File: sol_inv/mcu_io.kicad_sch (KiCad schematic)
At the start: 33 parts, among them J10 Conn_01x05, J3 Conn_01x06, J4 Conn_01x05, J5 Conn_ARM_JTAG_SWD_10, J6 Conn_01x02, J7 Conn_01x08, J8 Conn_01x08, J9 Conn_01x05, SW2 SW_Push_Dual, SW3 SW_Push_Dual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

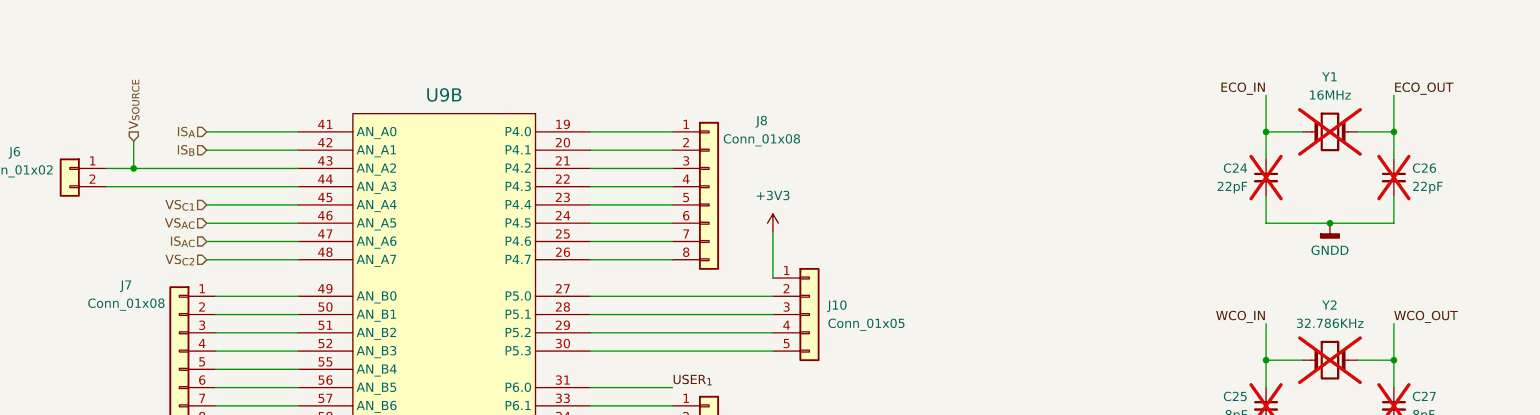
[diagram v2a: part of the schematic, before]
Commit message: v0.3 pcb layout pre-drc fixes
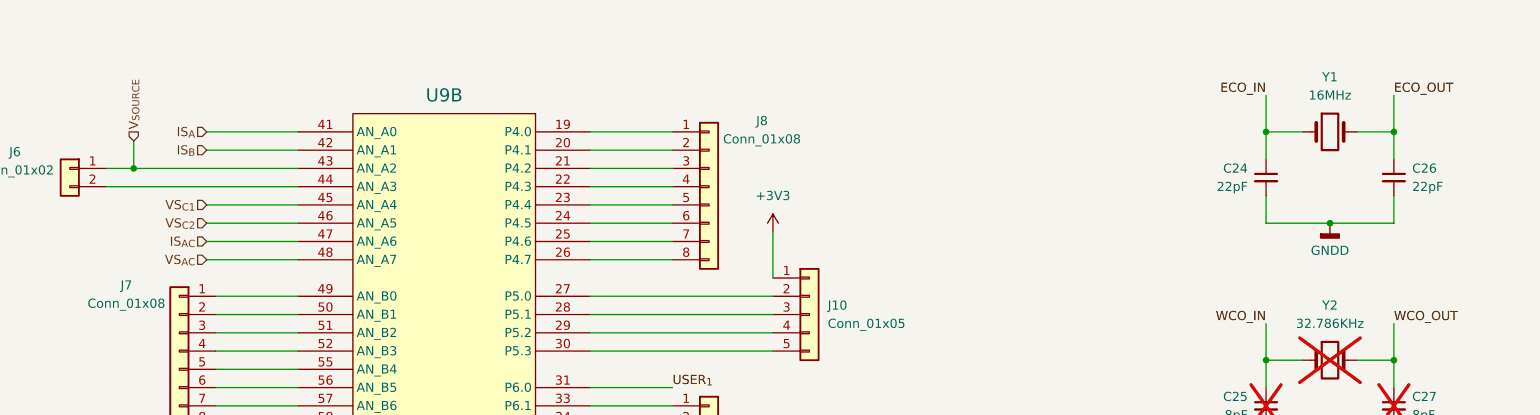
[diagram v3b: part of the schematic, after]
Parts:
- C21, C22, C23: footprint Capacitor_SMD:C_0201_0603Metric -> Capacitor_SMD:C_0402_1005Metric; ComponentLink2URL https://ro.farnell.com/wurth-elektronik/885012104002/cap-0-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 -> https://ro.farnell.com/kemet/c0402c104k4ractu/cap-0-1-f-16v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
- C24, C26: now fitted; now in the parts list
- Y1: footprint ABLS-16-000MHZ-B2-T:XTAL_ABLS-16_ABR -> SamacSys_Parts:ABLS7; ComponentLink2URL https://ro.farnell.com/abracon/abls-16-000mhz-d4-t/crystal-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 -> https://ro.mouser.com/ProductDetail/ABRACON/ABLS7M2-16.000M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; now fitted; now in the parts list
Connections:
- net VS_{AC}: now also U9.48 (AN_A7); no longer U9.46 (AN_A5)
- net VS_{C2}: now also U9.46 (AN_A5); no longer U9.48 (AN_A7)
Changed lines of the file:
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@@
 	(title_block
 		(title "MCU I/O")
-		(date "2025-04-24")
-		(rev "0.2.1")
+		(date "2025-05-01")
+		(rev "0.3")
 		(company "Cezar-Octavian Bontaș")
 	)
@@
 		)
 	)
+	(hierarchical_label "VS_{AC}"
+		(shape input)
+		(at 102.87 43.18 180)
+		(effects
+			(font
+				(size 1.27 1.27)
+			)
+			(justify right)
+		)
+	)
+	(hierarchical_label "VS_{C2}"
+		(shape input)
+		(at 102.87 38.1 180)
+		(effects
+			(font
+				(size 1.27 1.27)
+			)
+			(justify right)
+		)
+	)
 	(hierarchical_label "IN_{A}"
 		(shape output)
@@
 		)
 	)
-	(hierarchical_label "VS_{AC}"
-		(shape input)
-		(at 102.87 38.1 180)
-		(effects
-			(font
-				(size 1.27 1.27)
-			)
-			(justify right)
-		)
-	)
 	(hierarchical_label "IN_{B}"
 		(shape output)
@@
 		)
 	)
-	(hierarchical_label "VS_{C2}"
-		(shape input)
-		(at 102.87 43.18 180)
-		(effects
-			(font
-				(size 1.27 1.27)
-			)
-			(justify right)
-		)
-	)
 	(symbol
 		(lib_id "Device:C_Small")
@@
 			)
 		)
-		(property "Footprint" "Capacitor_SMD:C_0201_0603Metric"
+		(property "Footprint" "Capacitor_SMD:C_0402_1005Metric"
 			(at 30.48 147.0152 0)
 			(effects
@@
 			)
 		)
-		(property "Datasheet" "https://www.farnell.com/datasheets/3816100.pdf"
+		(property "Datasheet" "https://content.kemet.com/datasheets/KEM_C1002_X7R_SMD.pdf"
 			(at 34.29 146.05 0)
 			(effects
@@
 			)
 		)
-		(property "ComponentLink2URL" "https://ro.farnell.com/wurth-elektronik/885012104002/cap-0-1uf-10v-mlcc-0201/dp/4137872"
+		(property "ComponentLink2URL" "https://ro.farnell.com/kemet/c0402c104k4ractu/cap-0-1-f-16v-10-x7r-0402/dp/1288252"
 			(at 34.29 146.05 0)
 			(effects
@@
 		(unit 1)
 		(exclude_from_sim no)
-		(in_bom no)
+		(in_bom yes)
 		(on_board yes)
-		(dnp yes)
+		(dnp no)
 		(property "Reference" "C24"
 			(at 247.65 30.4862 0)
@@
 		(unit 1)
 		(exclude_from_sim no)
-		(in_bom no)
+		(in_bom yes)
 		(on_board yes)
-		(dnp yes)
+		(dnp no)
 		(fields_autoplaced yes)
 		(property "Reference" "C26"
@@
 			)
 		)
-		(property "Footprint" "Capacitor_SMD:C_0201_0603Metric"
+		(property "Footprint" "Capacitor_SMD:C_0402_1005Metric"
 			(at 238.76 125.73 0)
 			(effects
@@
 			)
 		)
-		(property "Datasheet" "https://www.farnell.com/datasheets/3816100.pdf"
+		(property "Datasheet" "https://content.kemet.com/datasheets/KEM_C1002_X7R_SMD.pdf"
 			(at 238.76 125.73 0)
 			(effects
@@
 			)
 		)
-		(property "ComponentLink2URL" "https://ro.farnell.com/wurth-elektronik/885012104002/cap-0-1uf-10v-mlcc-0201/dp/4137872"
+		(property "ComponentLink2URL" "https://ro.farnell.com/kemet/c0402c104k4ractu/cap-0-1-f-16v-10-x7r-0402/dp/1288252"
 			(at 238.76 125.73 0)
 			(effects
@@
 			)
 		)
-		(property "Footprint" "Capacitor_SMD:C_0201_0603Metric"
+		(property "Footprint" "Capacitor_SMD:C_0402_1005Metric"
 			(at 238.76 149.86 0)
 			(effects
@@
 			)
 		)
-		(property "Datasheet" "https://www.farnell.com/datasheets/3816100.pdf"
+		(property "Datasheet" "https://content.kemet.com/datasheets/KEM_C1002_X7R_SMD.pdf"
 			(at 238.76 149.86 0)
 			(effects
@@
 			)
 		)
-		(property "ComponentLink2URL" "https://ro.farnell.com/wurth-elektronik/885012104002/cap-0-1uf-10v-mlcc-0201/dp/4137872"
+		(property "ComponentLink2URL" "https://ro.farnell.com/kemet/c0402c104k4ractu/cap-0-1-f-16v-10-x7r-0402/dp/1288252"
 			(at 238.76 149.86 0)
 			(effects
@@
 		(unit 1)
 		(exclude_from_sim no)
-		(in_bom no)
+		(in_bom yes)
 		(on_board yes)
-		(dnp yes)
+		(dnp no)
 		(fields_autoplaced yes)
 		(property "Reference" "Y1"
@@
 			)
 		)
-		(property "Footprint" "ABLS-16-000MHZ-B2-T:XTAL_ABLS-16_ABR"
+		(property "Footprint" "SamacSys_Parts:ABLS7"
 			(at 259.08 25.4 0)
 			(effects
@@
 			)
 		)
-		(property "Datasheet" "https://4donline.ihs.com/images/VipMasterIC/IC/ABRC/ABRCS03441/ABRCS03441-1.pdf?hkey=6D3A4C79FDBF58556ACFDE234799DDF0"
+		(property "Datasheet" "https://ro.mouser.com/datasheet/2/3/ABLS7M2-1774905.pdf"
 			(at 259.08 25.4 0)
 			(effects
@@
 					(size 1.27 1.27)
 				)
+				(hide yes)
 			)
 		)
-		(property "ComponentLink2URL" "https://ro.farnell.com/abracon/abls-16-000mhz-d4-t/crystal-16mhz-18pf-11-5mm-x-4/dp/3819678"
+		(property "ComponentLink2URL" "https://ro.mouser.com/ProductDetail/ABRACON/ABLS7M2-16.000MHZ-D-2Y-T?qs=%252Bk6%2F5FB6qrnKBcQH%252BGT8Xw%3D%3D"
 			(at 259.08 25.4 0)
 			(effects
@@
 		(instances
 			(project ""
+				(path "/c5b733d3-d844-4c5a-a928-539beea9cfbc/53ef7f55-61e8-4ef7-94ec-bf64f13de35b"
+					(reference "Y1")
+					(unit 1)
+				)
 				(path "/c5b733d3-d844-4c5a-a928-539beea9cfbc/cfdc49a3-8c65-4747-bcf8-434cef8ee182"
 					(reference "Y1")

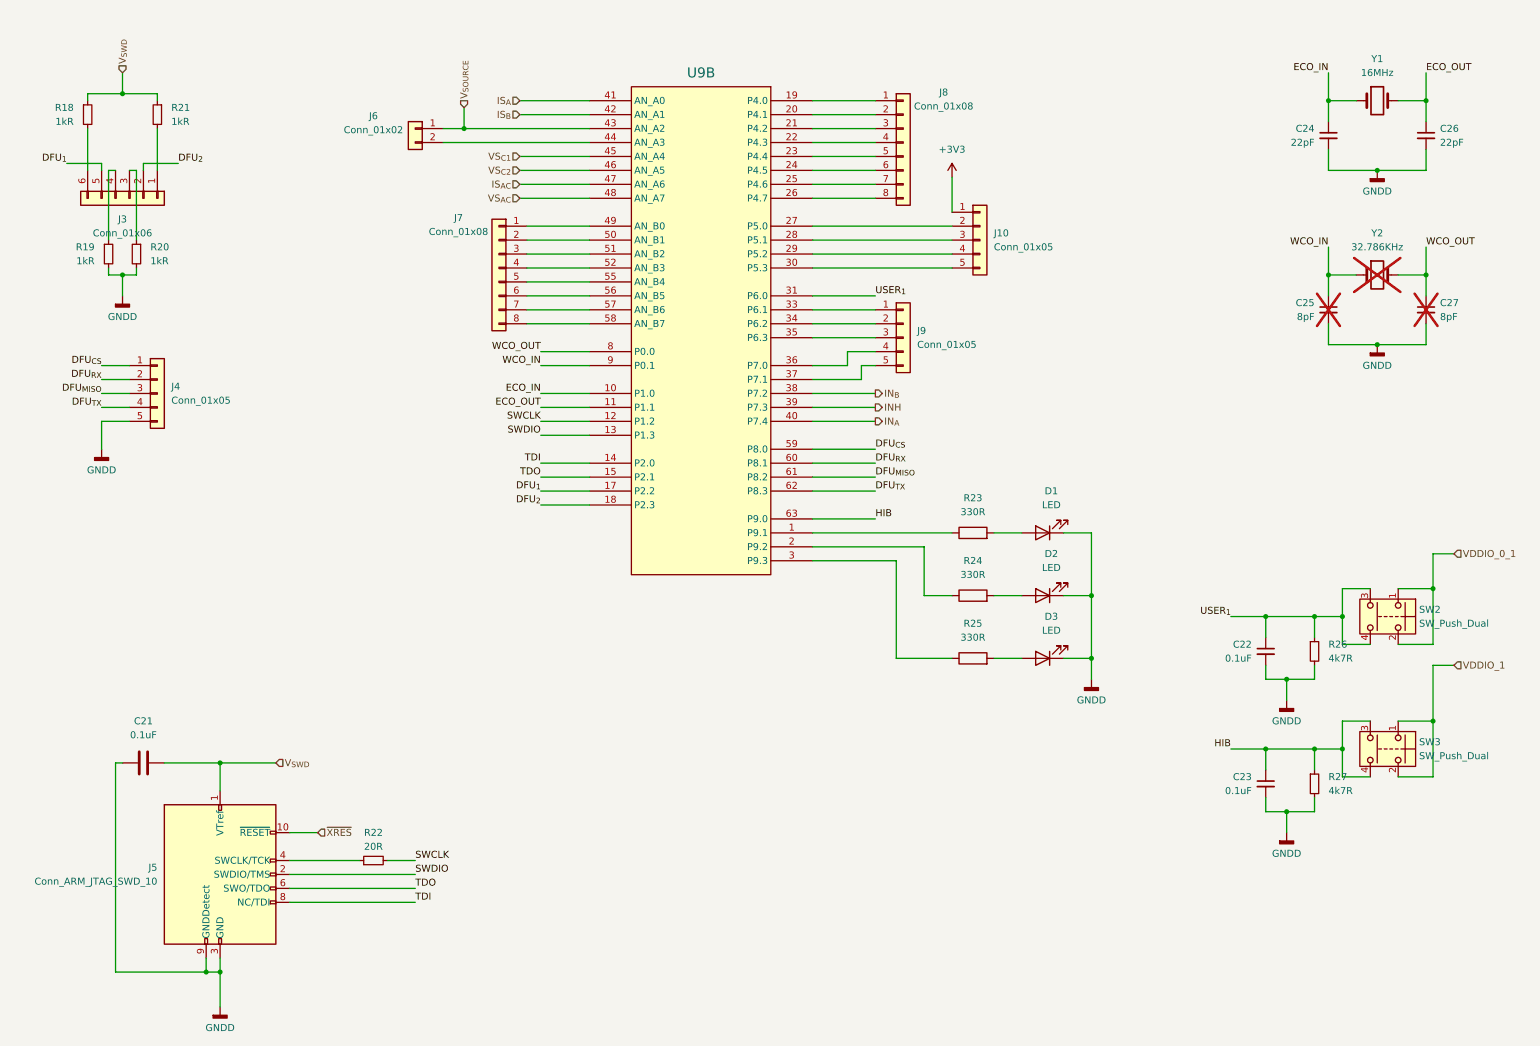
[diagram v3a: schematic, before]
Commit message: v0.3.4 fixes + component change for farnell
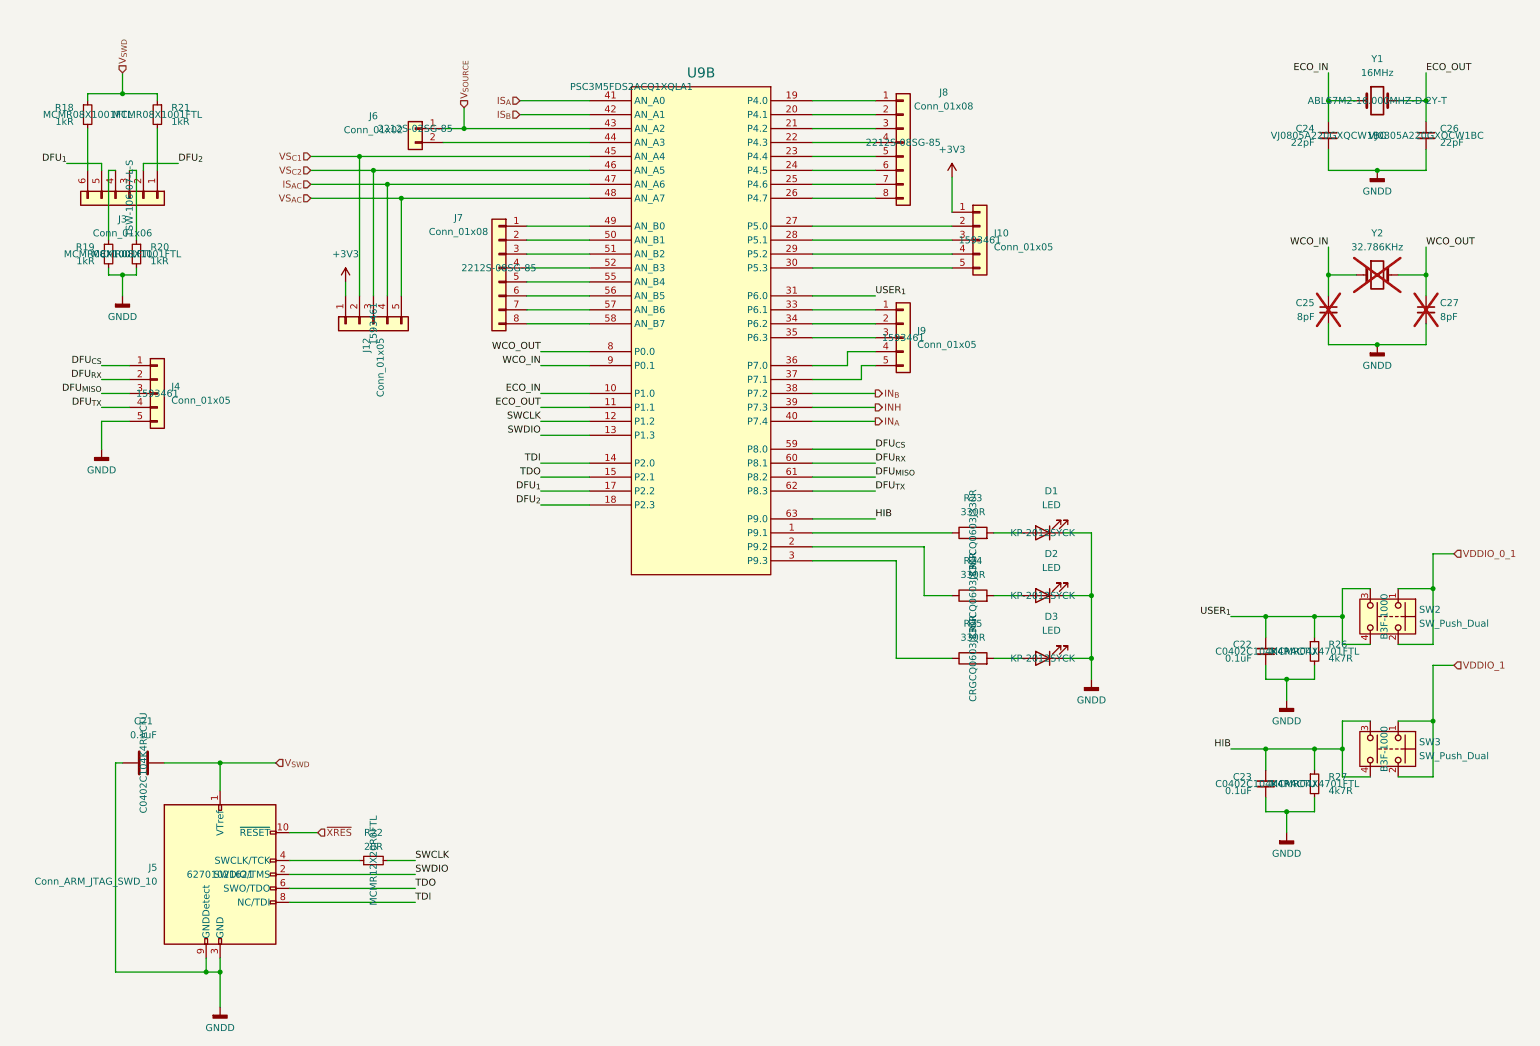
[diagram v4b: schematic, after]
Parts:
- added J12: Conn_01x05, Connector_PinSocket_2.54mm:PinSocket_1x05_P2.54mm_Vertical, symbol Connector_Generic:Conn_01x05
- C21, C22, C23: Manufacturer Part Number (none) -> C0402C104K4RACTU
- C24, C26: Manufacturer Part Number (none) -> VJ0805A220GXQCW1BC
- D1, D2, D3: Manufacturer Part Number (none) -> KP-2012SYCK
- J10, J4, J9: Manufacturer Part Number (none) -> 1593461
- J3: Manufacturer Part Number (none) -> TSW-106-07-L-S
- J5: Manufacturer Part Number (none) -> 62701021621
- J6: Manufacturer Part Number (none) -> 2212S-02SG-85
- J7, J8: Manufacturer Part Number (none) -> 2212S-08SG-85
- R18, R19, R20, R21: Manufacturer Part Number (none) -> MCMR08X1001FTL
- R22: Manufacturer Part Number (none) -> MCMR12X20R0FTL
- R23, R24, R25: Manufacturer Part Number (none) -> CRGCQ0603J330R
- R26, R27: Manufacturer Part Number (none) -> MCMR04X4701FTL
- SW2, SW3: Manufacturer Part Number (none) -> B3F-1000
- U9: Manufacturer Part Number (none) -> PSC3M5FDS2ACQ1XQLA1
- Y1: Manufacturer Part Number (none) -> ABLS7M2-16.000MHZ-D-2Y-T
- Y2: footprint LFXTAL002995:XTAL_LFXTAL002995BULK_IQD -> Crystal:Crystal_DS26_D2.0mm_L6.0mm_Vertical
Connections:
- net +3V3: now also J12.1 (Pin_1)
- net IS_{AC}: now also J12.4 (Pin_4)
- net VS_{AC}: now also J12.5 (Pin_5)
- net VS_{C1}: now also J12.2 (Pin_2)
- net VS_{C2}: now also J12.3 (Pin_3)

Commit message: v0.4 fixed mcu ldo part, production testing
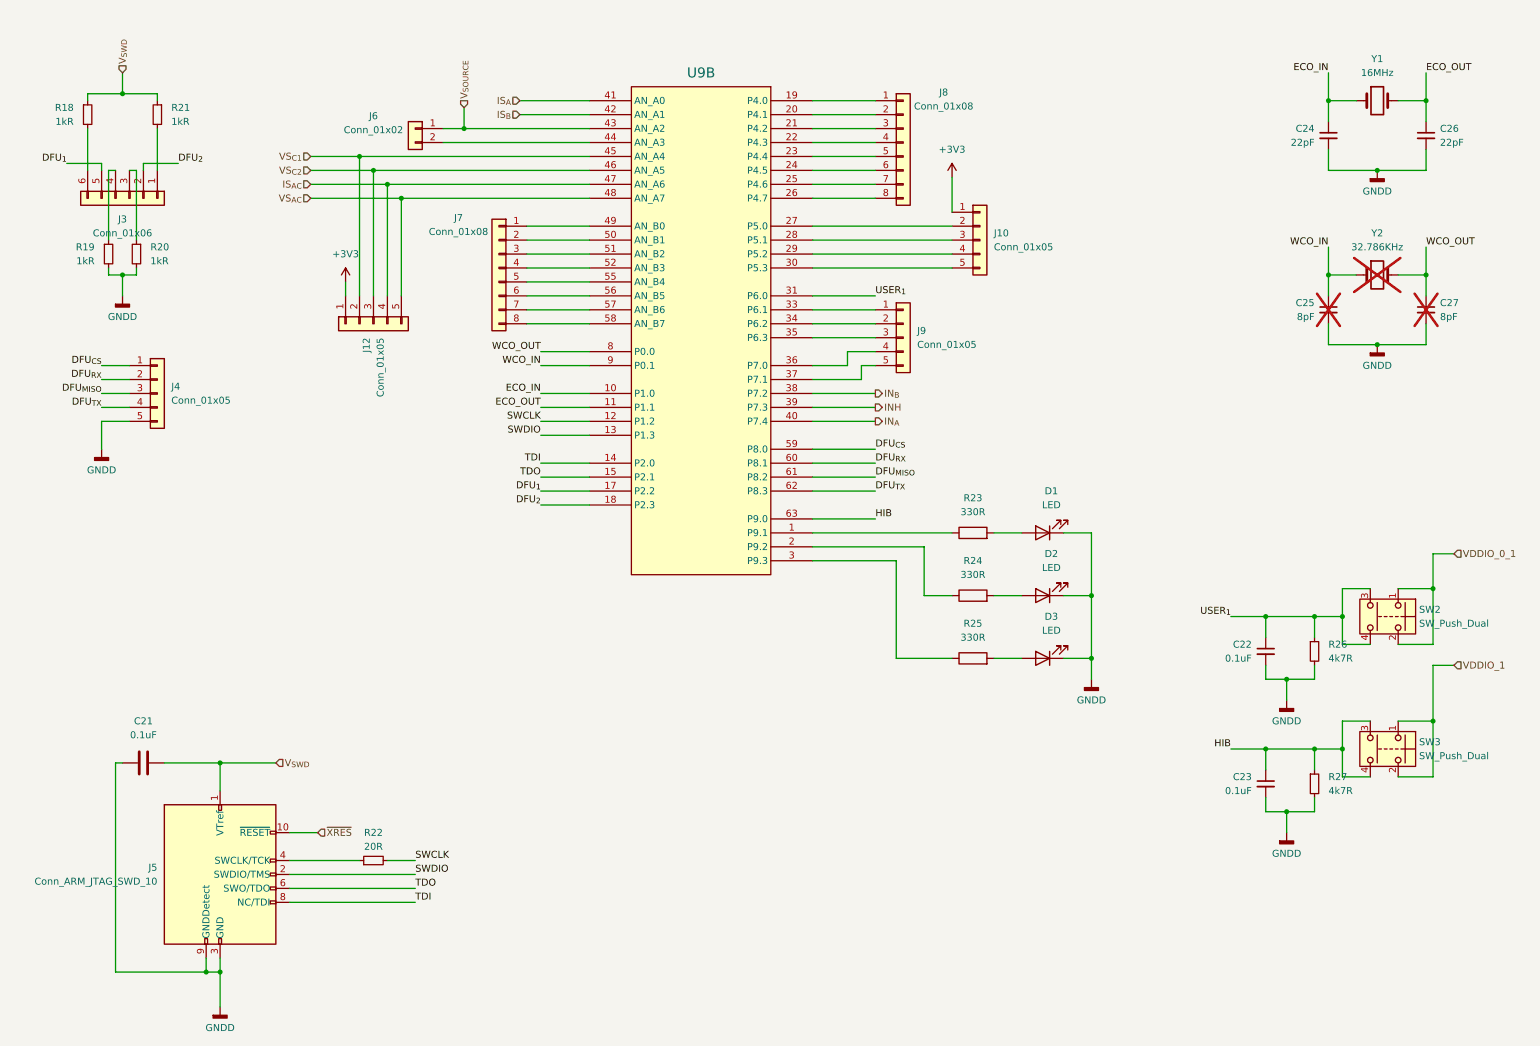
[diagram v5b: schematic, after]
